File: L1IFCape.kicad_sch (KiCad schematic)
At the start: 67 parts, among them J1 RF_Shield_One_Piece, J2 SMA, J3 MMCX, P8 BeagleBone_Black_Header, P9 BeagleBone_Black_Header, U1 24CS256, U2 MAX2769BETI+T, U3 MAX31343ETAY+T, U4 TPS717285DCK, U5 TPS717285DCK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

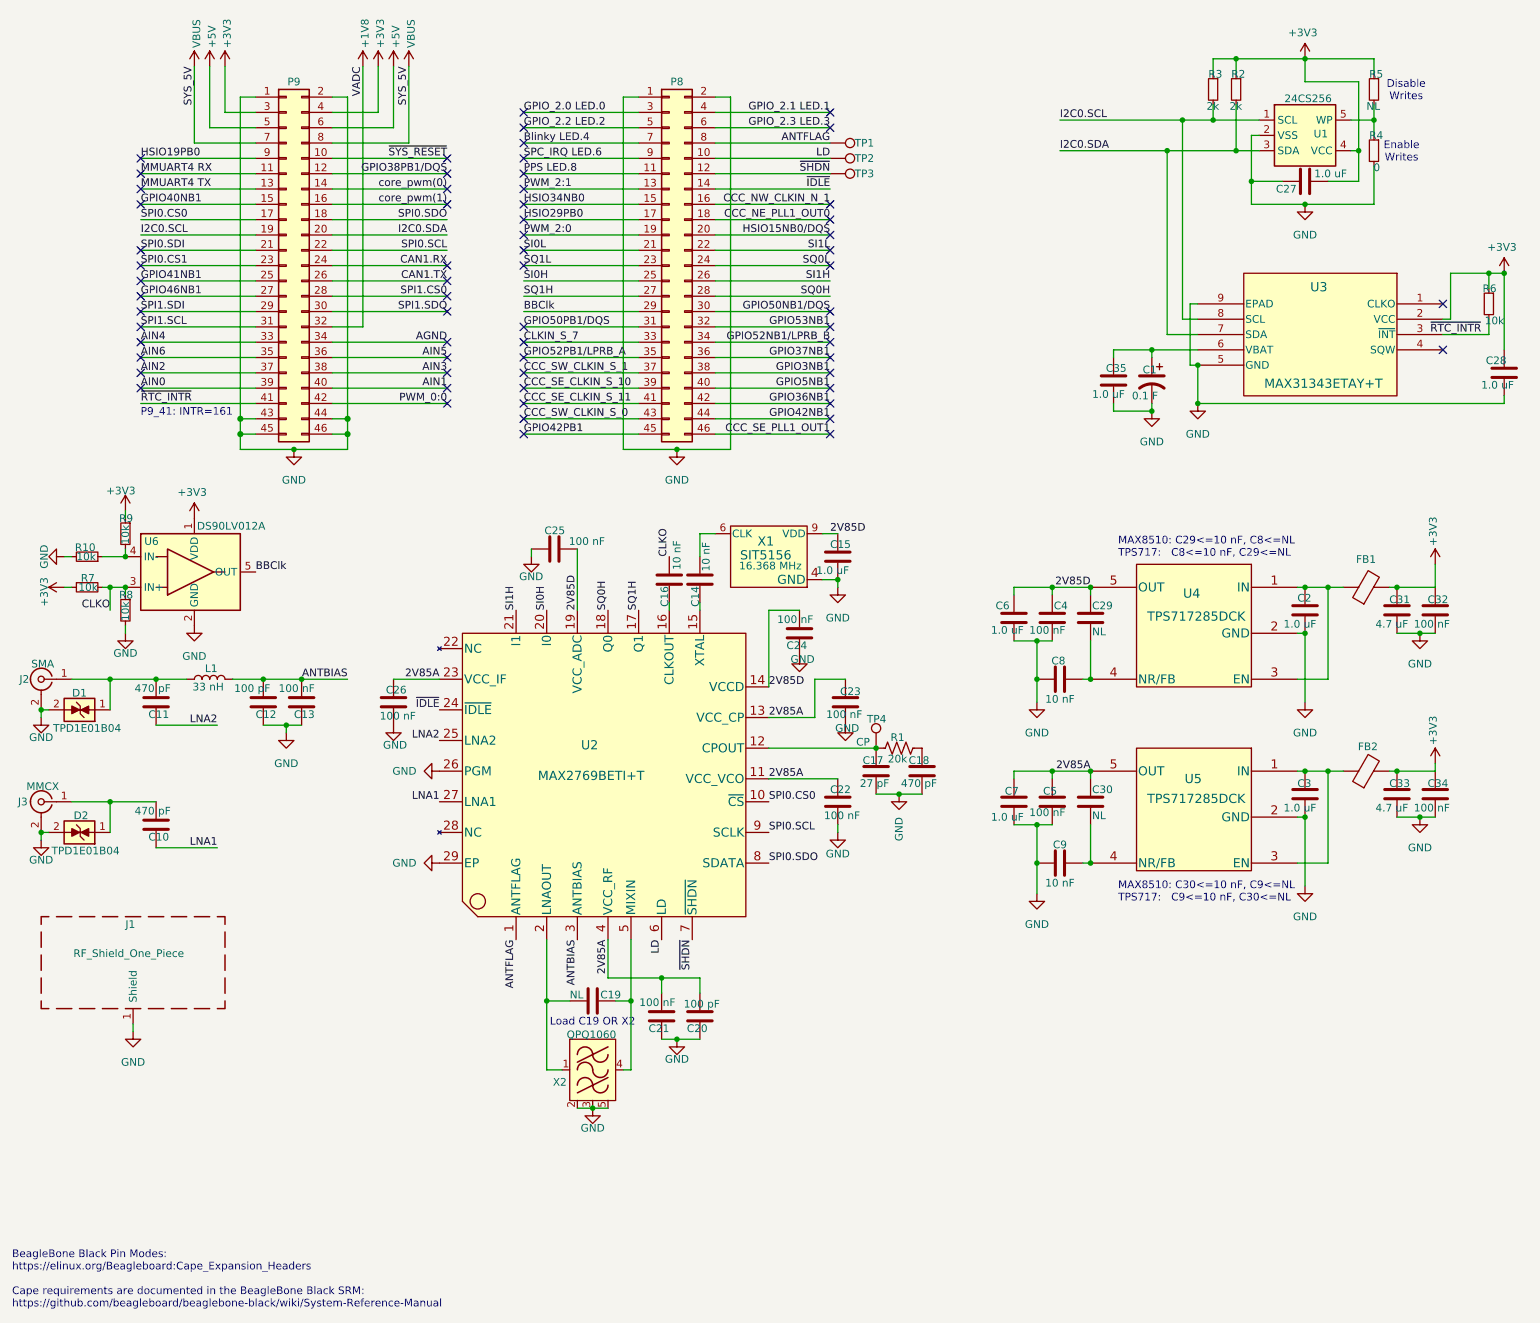
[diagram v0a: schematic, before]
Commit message: Added CERN License
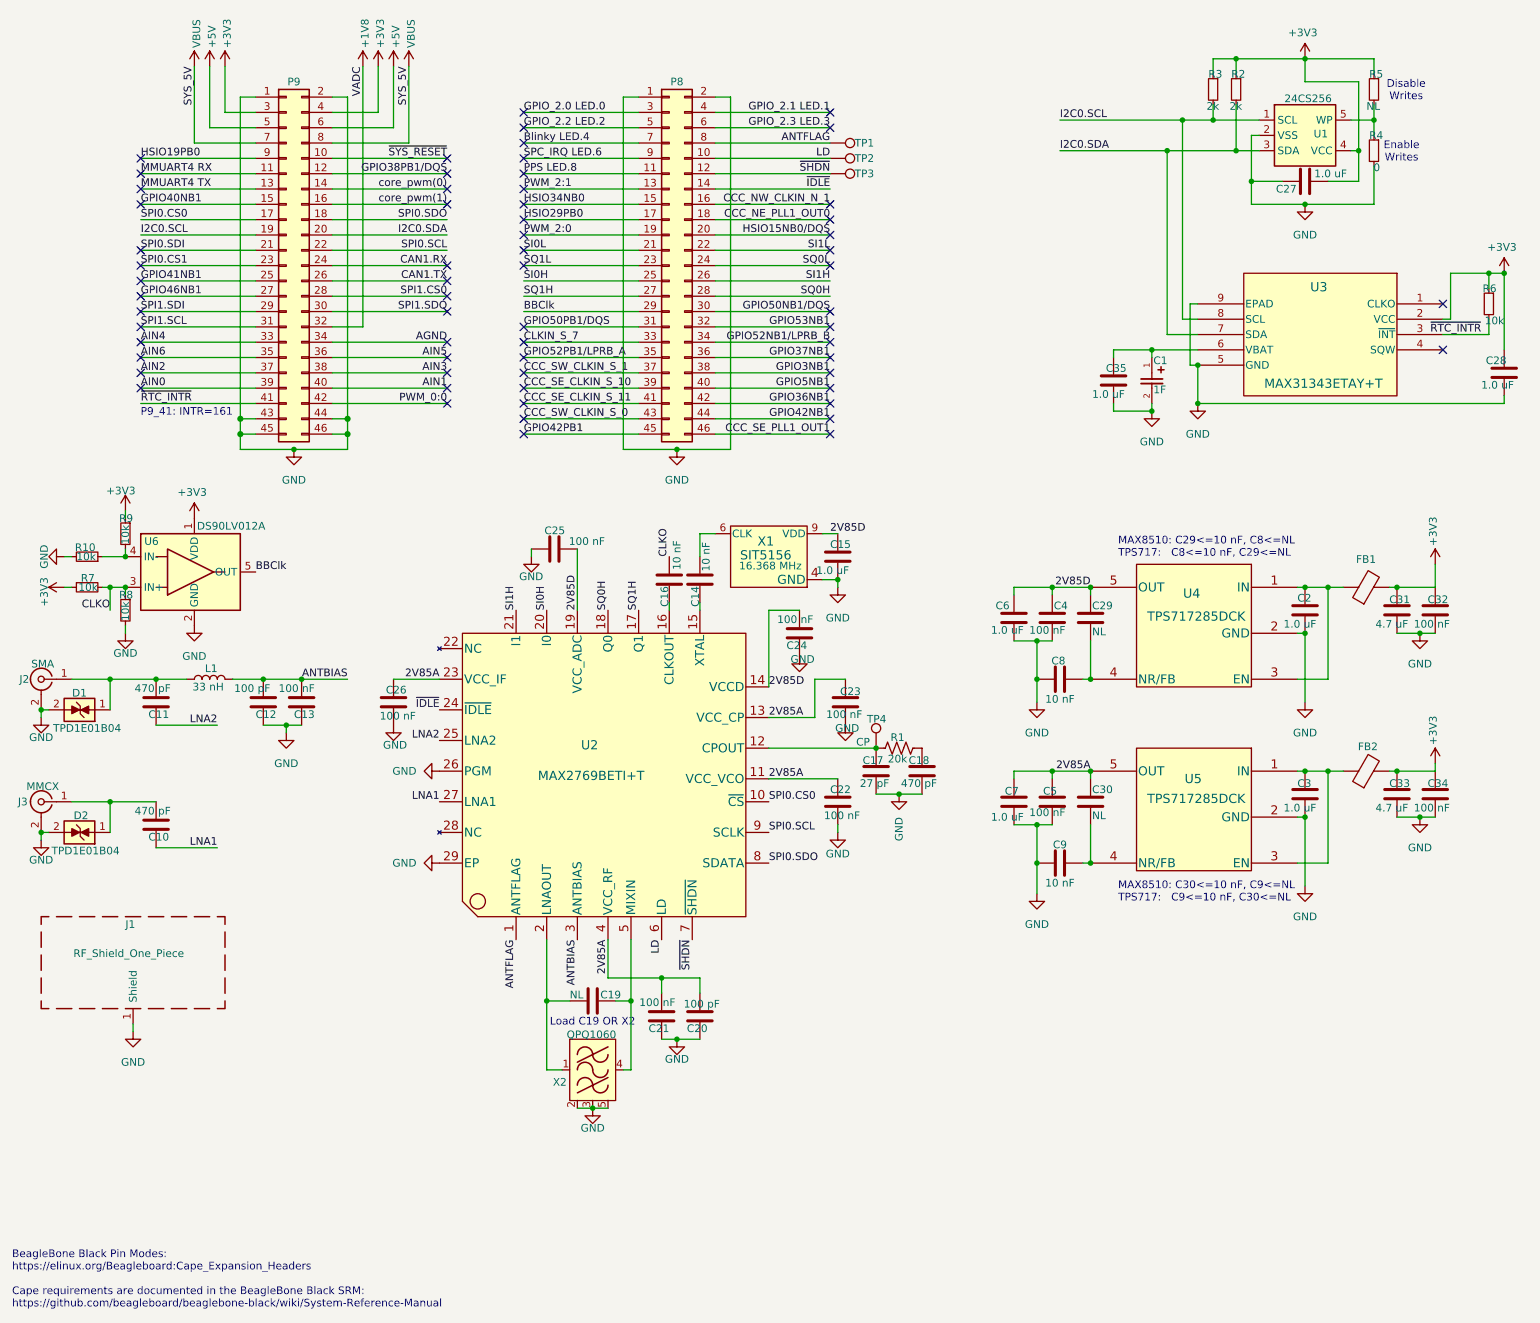
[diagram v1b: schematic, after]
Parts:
- removed C1: 0.1 F, L1IF:C_EDLC_FCR_10.8x10.8, symbol L1IF:C_Polarized_US
- added C1: 1F, L1IF:CAPPRD500W145D1350H830, symbol L1IF:KW-5R5C334-R
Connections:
- net GND: now also C1.2
- net at C35.1, U3.6 (VBAT): now also C1.1

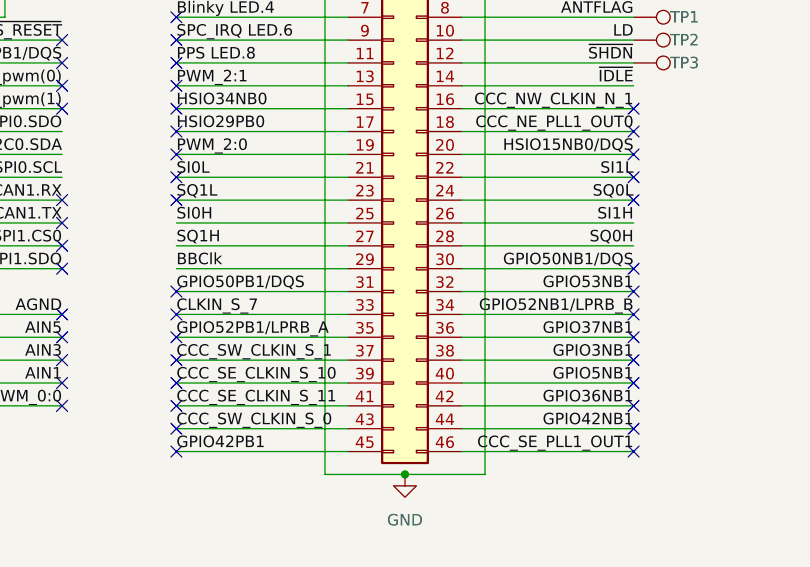
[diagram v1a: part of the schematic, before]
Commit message: Added Padlock graphic and 1F Supercap
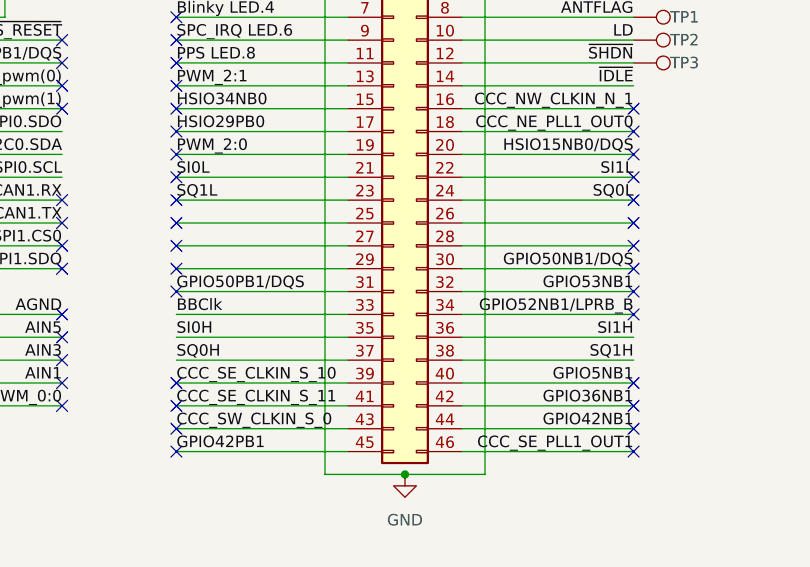
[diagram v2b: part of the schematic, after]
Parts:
- C1: footprint L1IF:CAPPRD500W145D1350H830 -> L1IF:KR5R5C105R; Availability In Stock -> (none); Check_prices https://www.snapeda.com/parts/KW-5R5C334-R/Eaton/view-part/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 -> (none); Description_1 Super Capacitor, Radial, Can, 330mF, 5.5V, 50Ohm, 1kHz, Thr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 -> (none); MANUFACTURER_NAME Eaton -> (none); MF Eaton -> (none); MFR (none) -> Eaton; MOUSER_PART_NUMBER 504-KW-5R5C334-R -> (none); MOUSER_PRICE-STOCK https://www.mouser.co.uk/ProductDetail/PowerStor-Eaton/KW-5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 -> (none); MP KW-5R5C334-R -> KR-5R5C105-R; MPN (none) -> KR-5R5C105-R; Manufacturer (none) -> Eaton; Price None -> (none); VPN (none) -> 283-KR-5R5C105-R-ND; Vendor (none) -> DigiKey; Vendor PN (none) -> 283-KR-5R5C105-R-ND
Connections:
- net CCC_SW_CLKIN_S_1 is gone; now on net SQ0H: P8.37 (Pin_37)
- net CLKIN_S_7 is gone; now on net BBClk: P8.33 (Pin_33)
- net GPIO37NB1 is gone; now on net SI1H: P8.36 (Pin_36)
- net GPIO3NB1 is gone; now on net SQ1H: P8.38 (Pin_38)
- net GPIO52PB1/LPRB_A is gone; now on net SI0H: P8.35 (Pin_35)
- net BBClk: no longer P8.29 (Pin_29)
- net SI0H: no longer P8.25 (Pin_25)
- net SI1H: no longer P8.26 (Pin_26)
- net SQ0H: no longer P8.28 (Pin_28)
- net SQ1H: no longer P8.27 (Pin_27)

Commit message: Shorter Header Pins
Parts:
- P8, P9: MPN SSQ-123-03-G-D -> SSQ-123-02-G-D; Vendor PN SAM1196-23-ND -> SAM1185-23-ND
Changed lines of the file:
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@@
 			)
 		)
-		(property "MPN" "SSQ-123-03-G-D"
+		(property "MPN" "SSQ-123-02-G-D"
 			(at 62.23 57.15 0)
 			(effects
@@
 			)
 		)
-		(property "Vendor PN" "SAM1196-23-ND"
+		(property "Vendor PN" "SAM1185-23-ND"
 			(at 62.23 57.15 0)
 			(effects
@@
 			)
 		)
-		(property "MPN" "SSQ-123-03-G-D"
+		(property "MPN" "SSQ-123-02-G-D"
 			(at 125.73 57.15 0)
 			(effects
@@
 			)
 		)
-		(property "Vendor PN" "SAM1196-23-ND"
+		(property "Vendor PN" "  SAM1185-23-ND"
 			(at 125.73 57.15 0)
 			(effects

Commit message: Ordered Rev2 from OSH Park
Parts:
- P8: Vendor PN SAM1185-23-ND -> SAM1185-23-ND

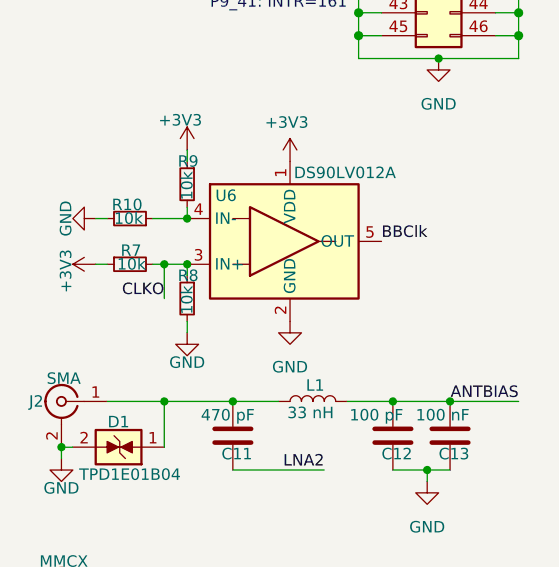
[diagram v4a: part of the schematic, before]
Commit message: Moved Antenna Ports, and changed resistor bias circuit
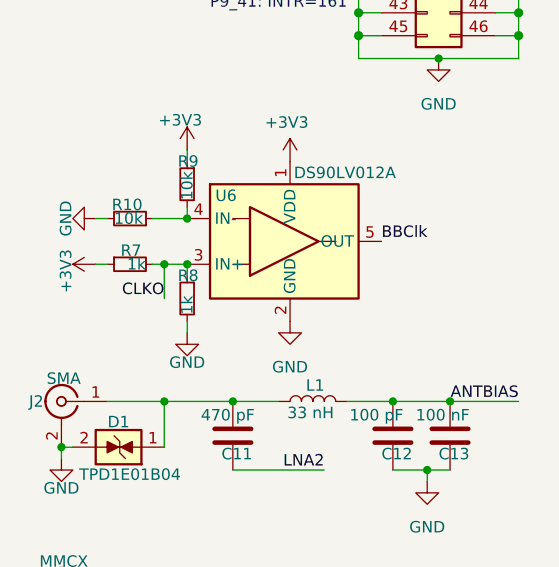
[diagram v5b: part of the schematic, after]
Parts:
- P8, P9: MPN SSQ-123-02-G-D -> SSQ-123-23-G-D; Vendor PN SAM1185-23-ND -> 612-SSQ-123-23-G-D-ND
- R7, R8: value 10k -> 1k; MPN ERJ-3EKF1002V -> ERJ-3EKF1001V; Vendor PN P10.0KHCT-ND -> P1.00KHCT-ND
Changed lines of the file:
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@@
 			)
 		)
-		(property "Datasheet" "https://mm.digikey.com/Volume0/opasdata/d220001/medias/docus/6129/ssq-1xx-xx-xxx-x-xx-xxx-xx-x-mkt.pdf"
+		(property "Datasheet" "https://suddendocs.samtec.com/catalog_english/ssq_th.pdf"
 			(at 62.23 78.74 0)
 			(hide yes)
@@
 			)
 		)
-		(property "MPN" "SSQ-123-02-G-D"
+		(property "MPN" "SSQ-123-23-G-D"
 			(at 62.23 57.15 0)
 			(hide yes)
@@
 			)
 		)
-		(property "Vendor PN" "SAM1185-23-ND"
+		(property "Vendor PN" "612-SSQ-123-23-G-D-ND"
 			(at 62.23 57.15 0)
 			(hide yes)
@@
 			)
 		)
-		(property "Datasheet" "https://mm.digikey.com/Volume0/opasdata/d220001/medias/docus/6129/ssq-1xx-xx-xxx-x-xx-xxx-xx-x-mkt.pdf"
+		(property "Datasheet" "https://suddendocs.samtec.com/catalog_english/ssq_th.pdf"
 			(at 125.73 78.74 0)
 			(hide yes)
@@
 			)
 		)
-		(property "MPN" "SSQ-123-02-G-D"
+		(property "MPN" "SSQ-123-23-G-D"
 			(at 125.73 57.15 0)
 			(hide yes)
@@
 			)
 		)
-		(property "Vendor PN" "SAM1185-23-ND"
+		(property "Vendor PN" "612-SSQ-123-23-G-D-ND"
 			(at 125.73 57.15 0)
 			(hide yes)
@@
 			)
 		)
-		(property "Value" "10k"
+		(property "Value" "1k"
 			(at 35.56 116.078 90)
 			(show_name no)
@@
 			)
 		)
-		(property "Datasheet" ""
+		(property "Datasheet" "https://industrial.panasonic.com/cdbs/www-data/pdf/RDA0000/AOA0000C304.pdf"
 			(at 35.56 114.3 0)
 			(hide yes)
@@
 			)
 		)
-		(property "Description" "RES SMD 10K OHM 1% 1/10W 0603"
+		(property "Description" "RES SMD 1K OHM 1% 1/10W 0603"
 			(at 35.56 114.3 0)
 			(hide yes)
@@
 			)
 		)
-		(property "MPN" "ERJ-3EKF1002V"
+		(property "MPN" "ERJ-3EKF1001V"
 			(at 35.56 114.3 0)
 			(hide yes)
@@
 			)
 		)
-		(property "Vendor PN" "P10.0KHCT-ND"
+		(property "Vendor PN" "P1.00KHCT-ND"
 			(at 35.56 114.3 0)
 			(hide yes)
@@
 			)
 		)
-		(property "Value" "10k"
+		(property "Value" "1k"
 			(at 30.988 110.49 90)
 			(show_name no)
@@
 			)
 		)
-		(property "Datasheet" ""
+		(property "Datasheet" "https://industrial.panasonic.com/cdbs/www-data/pdf/RDA0000/AOA0000C304.pdf"
 			(at 29.21 110.49 0)
 			(hide yes)
@@
 			)
 		)
-		(property "Description" "RES SMD 10K OHM 1% 1/10W 0603"
+		(property "Description" "RES SMD 1K OHM 1% 1/10W 0603"
 			(at 29.21 110.49 0)
 			(hide yes)
@@
 			)
 		)
-		(property "MPN" "ERJ-3EKF1002V"
+		(property "MPN" "ERJ-3EKF1001V"
 			(at 29.21 110.49 0)
 			(hide yes)
@@
 			)
 		)
-		(property "Vendor PN" "P10.0KHCT-ND"
+		(property "Vendor PN" "P1.00KHCT-ND"
 			(at 29.21 110.49 0)
 			(hide yes)
